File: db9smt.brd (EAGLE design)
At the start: 33.5 x 18.5 mm, 20 parts, among them CON1 PADONPRINT, CON2 PADONPRINT, CON3 PADONPRINT, CON4 PADONPRINT, CON5 PADONPRINT, CON6 PADONPRINT, CON7 PADONPRINT, CON8 PADONPRINT, CON9 PADONPRINT

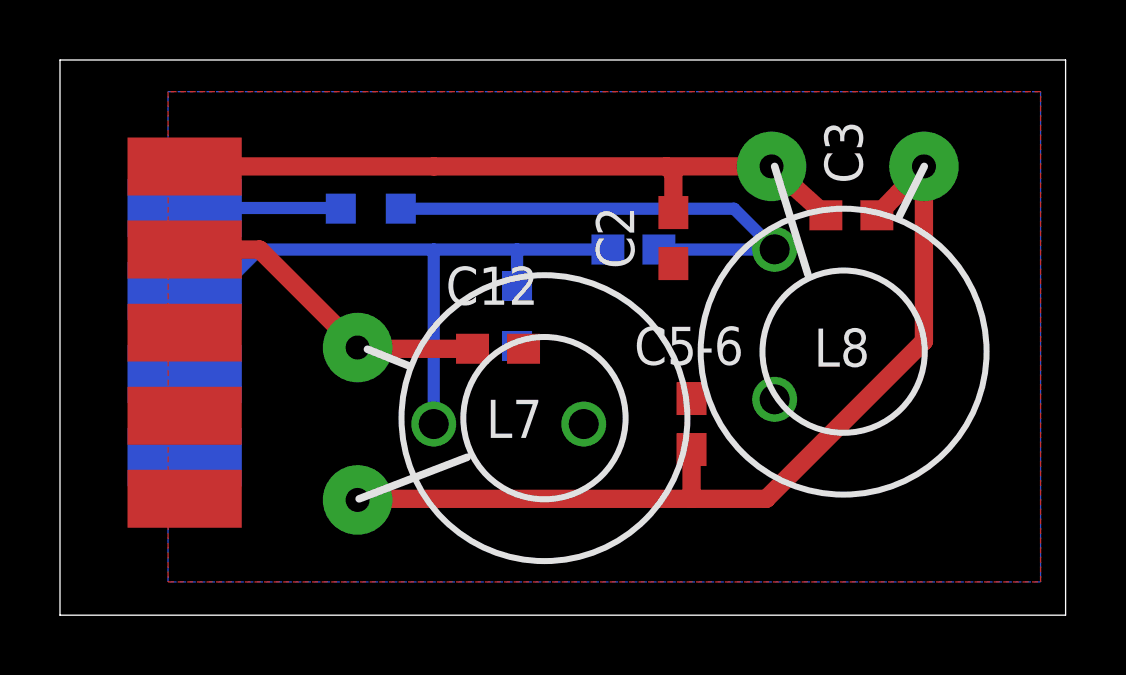
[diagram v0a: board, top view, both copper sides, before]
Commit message: Smaller board
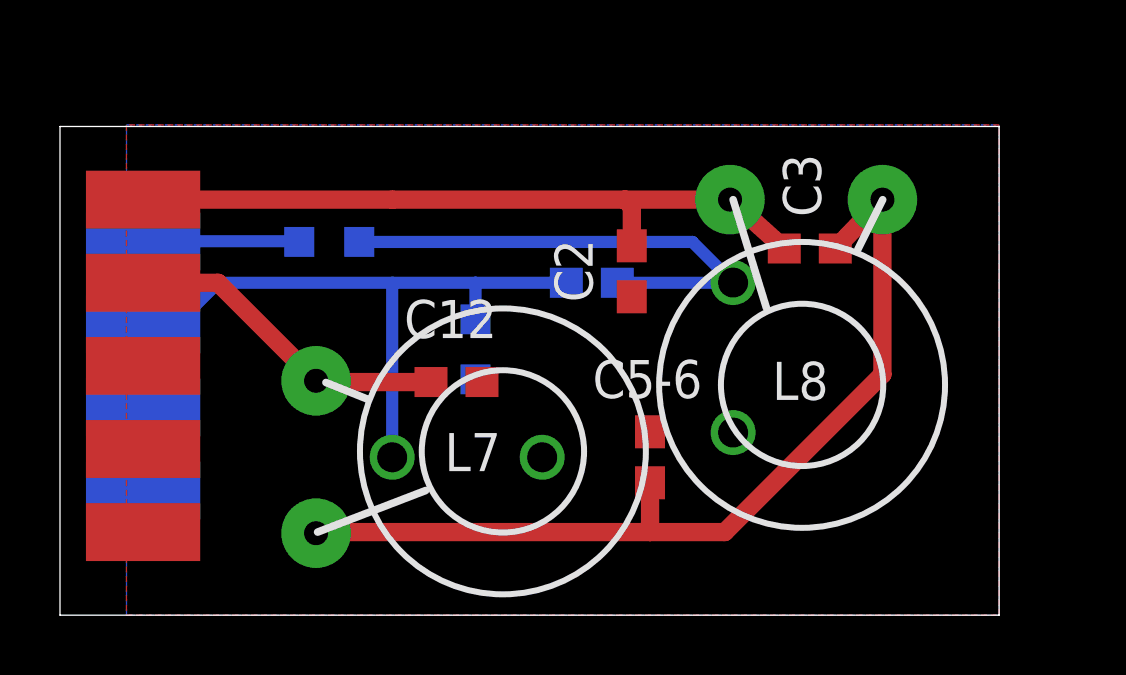
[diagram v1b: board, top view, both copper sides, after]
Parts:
- moved C2 1.77 mm to (19.1, 11.5)
- moved C3 1.77 mm to (25.0, 12.2)
- moved L8 1.77 mm to (22.3, 13.9)
- moved C12 1.77 mm to (13.2, 7.77)
- moved CON1 1.77 mm to (2.77, 13.8)
- moved CON2 1.77 mm to (2.77, 11.1)
- moved CON6 1.77 mm to (2.77, 12.5)
- moved CON7 1.77 mm to (2.77, 9.70)
- moved CON5 1.77 mm to (2.77, 2.77)
- moved CT2 1.77 mm to (13.6, 5.26)
- moved L7 1.77 mm to (8.54, 2.73)
- moved CON4 1.77 mm to (2.77, 5.54)
- moved CON8 1.77 mm to (2.77, 6.92)
- moved CON9 1.77 mm to (2.77, 4.16)
- moved CON3 1.77 mm to (2.77, 8.31)
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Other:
- board size 33.5 x 18.5 mm -> 31.3 x 16.3 mm
